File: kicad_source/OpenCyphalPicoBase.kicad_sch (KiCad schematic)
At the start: 48 parts, among them CN1 RASPBERRYPI_PICO, CN11 CONN_02X03, CN12 Conn_01x03, CN2 SM04B-SRSS-TB, CN3 SM04B-SRSS-TB, CN6 691322310002, CN7 CONN_02X03, CN8 Conn_02x08_Odd_Even, SW1 SPST, U3 24LC64

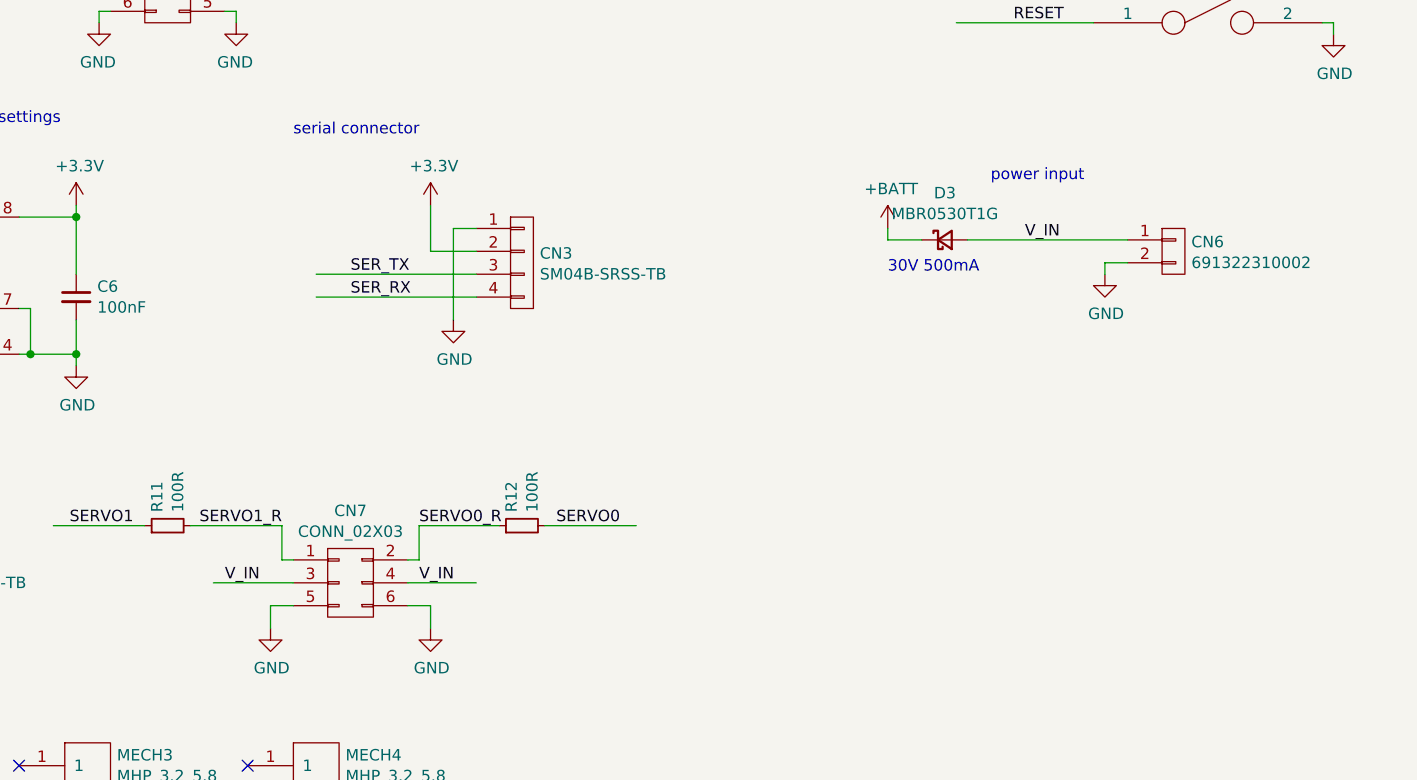
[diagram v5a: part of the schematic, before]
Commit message: switched servos to +BATT to power them from CAN bus
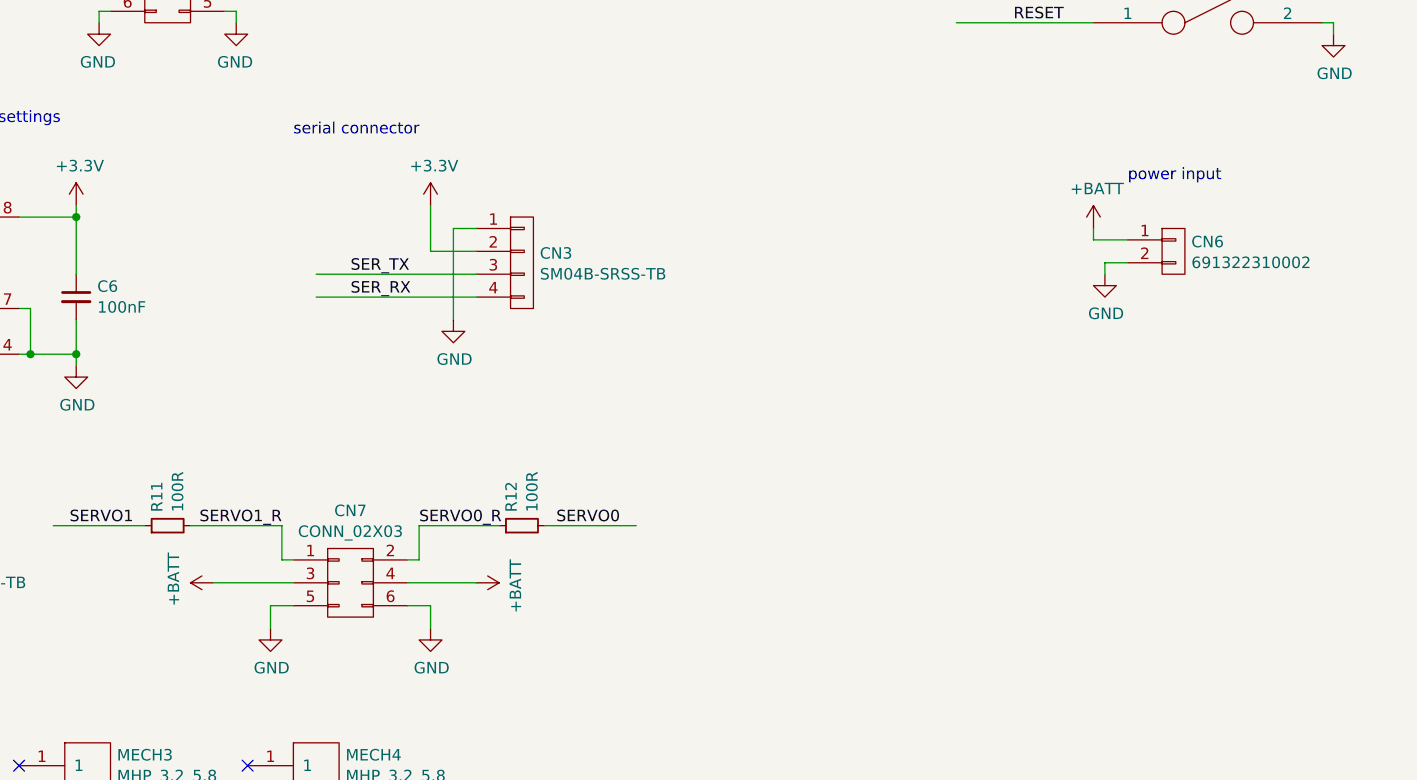
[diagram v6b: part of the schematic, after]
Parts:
- removed D3: MBR0530T1G, Diode_SMD:D_SOD-123, symbol Device:D_Schottky_Small
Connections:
- net V_IN is gone; now on net +BATT: CN6.1 (P1), CN7.3 (P3), CN7.4 (P4)
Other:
- note removed: "30V 500mA"
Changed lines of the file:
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@@
   (title_block
     (title "OpenCyphalPicoBase")
-    (date "2022-10-23")
+    (date "2022-10-24")
     (rev "0.2")
     (company "generationmake")
@@
     (stroke (width 0) (type default) (color 0 0 0 0))
   )
-  (wire (pts (xy 165.1 134.62) (xy 165.1 133.35))
+  (wire (pts (xy 187.96 134.62) (xy 187.96 133.35))
     (stroke (width 0) (type default) (color 0 0 0 0))
   )
@@
     (stroke (width 0) (type default) (color 0 0 0 0))
   )
-  (wire (pts (xy 168.91 134.62) (xy 165.1 134.62))
+  (wire (pts (xy 191.77 134.62) (xy 187.96 134.62))
     (stroke (width 0) (type default) (color 0 0 0 0))
   )
@@
     (stroke (width 0) (type default) (color 0 0 0 0))
   )
-  (wire (pts (xy 191.77 134.62) (xy 173.99 134.62))
-    (stroke (width 0) (type default) (color 0 0 0 0))
-  )
   (wire (pts (xy 116.84 41.91) (xy 116.84 39.37))
     (stroke (width 0) (type default) (color 0 0 0 0))
@@
     (effects (font (size 1.27 1.27)) (justify left bottom))
   )
-  (text "30V 500mA" (at 165.1 138.43 0)
-    (effects (font (size 1.27 1.27)) (justify left bottom))
-  )
   (text "I2C address: 0x50" (at 48.26 124.46 0)
     (effects (font (size 1.27 1.27)) (justify left bottom))
@@
     (effects (font (size 1.27 1.27)) (justify left bottom))
   )
-  (text "power input" (at 176.53 128.27 0)
+  (text "power input" (at 191.77 128.27 0)
     (effects (font (size 1.27 1.27)) (justify left bottom))
   )
@@
     (effects (font (size 1.27 1.27)) (justify left bottom))
   )
-  (label "V_IN" (at 91.44 172.72 0)
-    (effects (font (size 1.27 1.27)) (justify left bottom))
-  )
   (label "RESERVED0" (at 45.72 104.14 180)
     (effects (font (size 1.27 1.27)) (justify right bottom))
@@
     (effects (font (size 1.27 1.27)) (justify left bottom))
   )
-  (label "V_IN" (at 180.34 134.62 0)
-    (effects (font (size 1.27 1.27)) (justify left bottom))
-  )
   (label "SERVO1" (at 81.28 166.37 180)
     (effects (font (size 1.27 1.27)) (justify right bottom))
@@
   (label "OUTPUT1" (at 76.2 66.04 180)
     (effects (font (size 1.27 1.27)) (justify right bottom))
-  )
-  (label "V_IN" (at 113.03 172.72 0)
-    (effects (font (size 1.27 1.27)) (justify left bottom))
   )
   (label "SER_TX" (at 105.41 138.43 0)
@@
     (pin "1")
   )
-  (symbol (lib_id "Device:D_Schottky_Small") (at 171.45 134.62 0) (unit 1)
-    (in_bom yes) (on_board yes)
-    (property "Reference" "D3" (id 0) (at 171.45 129.413 0))
-    (property "Value" "MBR0530T1G" (id 1) (at 171.45 131.7244 0))
-    (property "Footprint" "Diode_SMD:D_SOD-123" (id 2) (at 171.45 134.62 90)
-      (effects (font (size 1.27 1.27)) hide)
-    )
-    (property "Datasheet" "" (id 3) (at 171.45 134.62 90))
-    (pin "1")
-    (pin "2")
-  )
-  (symbol (lib_id "OpenCyphalPicoBase-rescue:+BATT-power-supply") (at 165.1 133.35 0) (unit 1)
-    (in_bom yes) (on_board yes)
-    (property "Reference" "#PWR020" (id 0) (at 165.1 137.16 0)
-      (effects (font (size 1.27 1.27)) hide)
-    )
-    (property "Value" "+BATT" (id 1) (at 165.481 128.9558 0))
-    (property "Footprint" "" (id 2) (at 165.1 133.35 0))
-    (property "Datasheet" "" (id 3) (at 165.1 133.35 0))
+  (symbol (lib_id "OpenCyphalPicoBase-rescue:+BATT-power-supply") (at 187.96 133.35 0) (unit 1)
+    (in_bom yes) (on_board yes)
+    (property "Reference" "#PWR020" (id 0) (at 187.96 137.16 0)
+      (effects (font (size 1.27 1.27)) hide)
+    )
+    (property "Value" "+BATT" (id 1) (at 188.341 128.9558 0))
+    (property "Footprint" "" (id 2) (at 187.96 133.35 0))
+    (property "Datasheet" "" (id 3) (at 187.96 133.35 0))
     (pin "1")
   )
@@
     (pin "3")
   )
+  (symbol (lib_id "OpenCyphalPicoBase-rescue:+BATT-power-supply") (at 119.38 172.72 270) (unit 1)
+    (in_bom yes) (on_board yes)
+    (property "Reference" "#PWR0105" (id 0) (at 115.57 172.72 0)
+      (effects (font (size 1.27 1.27)) hide)
+    )
+    (property "Value" "+BATT" (id 1) (at 123.7742 173.101 0))
+    (property "Footprint" "" (id 2) (at 119.38 172.72 0))
+    (property "Datasheet" "" (id 3) (at 119.38 172.72 0))
+    (pin "1")
+  )
+  (symbol (lib_id "OpenCyphalPicoBase-rescue:+BATT-power-supply") (at 90.17 172.72 90) (unit 1)
+    (in_bom yes) (on_board yes)
+    (property "Reference" "#PWR0104" (id 0) (at 93.98 172.72 0)
+      (effects (font (size 1.27 1.27)) hide)
+    )
+    (property "Value" "+BATT" (id 1) (at 85.7758 172.339 0))
+    (property "Footprint" "" (id 2) (at 90.17 172.72 0))
+    (property "Datasheet" "" (id 3) (at 90.17 172.72 0))
+    (pin "1")
+  )
   (symbol (lib_id "OpenCyphalPicoBase-rescue:+BATT-power-supply") (at 165.1 92.71 0) (unit 1)
     (in_bom yes) (on_board yes)
@@
       (reference "#PWR0103") (unit 1) (value "GND") (footprint "")
     )
+    (path "/7e1637aa-4921-498b-900f-5fdac7ab5374"
+      (reference "#PWR0104") (unit 1) (value "+BATT") (footprint "")
+    )
+    (path "/5573649e-80ef-4e35-960b-dc18f9188f02"
+      (reference "#PWR0105") (unit 1) (value "+BATT") (footprint "")
+    )
     (path "/00000000-0000-0000-0000-000062a11dbe"
       (reference "C1") (unit 1) (value "100nF") (footprint "Capacitor_SMD:C_0603_1608Metric")
@@
       (reference "D2") (unit 1) (value "MBR0530T1G") (footprint "Diode_SMD:D_SOD-123")
     )
-    (path "/00000000-0000-0000-0000-000062533088"
-      (reference "D3") (unit 1) (value "MBR0530T1G") (footprint "Diode_SMD:D_SOD-123")
-    )
     (path "/00000000-0000-0000-0000-000062572e1d"

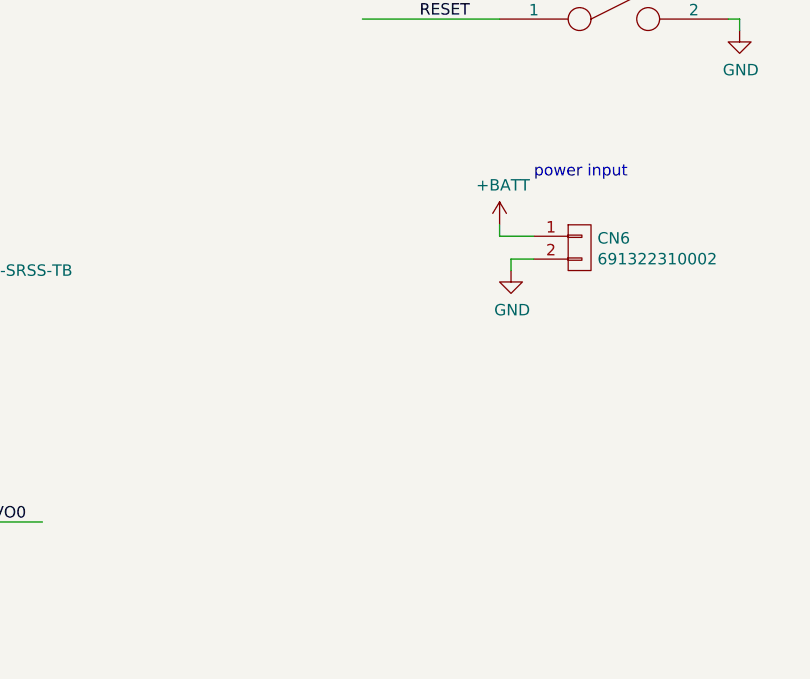
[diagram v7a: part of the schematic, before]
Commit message: added capacitor on +BATT
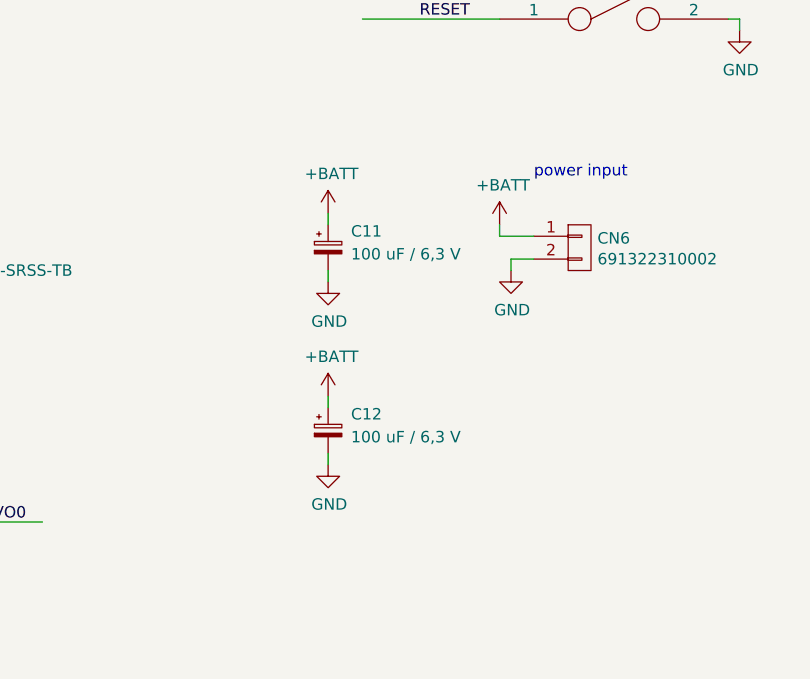
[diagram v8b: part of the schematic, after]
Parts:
- added C11, C12: 100 uF / 6,3 V, Capacitor_SMD:CP_Elec_5x5.3, symbol Device:C_Polarized_Small
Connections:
- net +BATT: now also C11.1, C12.1
- net GND: now also C11.2, C12.2
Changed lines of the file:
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@@
   (title_block
     (title "OpenCyphalPicoBase")
-    (date "2022-10-24")
+    (date "2022-10-26")
     (rev "0.2")
     (company "generationmake")
@@
     (stroke (width 0) (type default) (color 0 0 0 0))
   )
+  (wire (pts (xy 168.91 152.4) (xy 168.91 153.67))
+    (stroke (width 0) (type default) (color 0 0 0 0))
+  )
   (wire (pts (xy 19.05 36.83) (xy 21.59 36.83))
     (stroke (width 0) (type default) (color 0 0 0 0))
@@
     (stroke (width 0) (type default) (color 0 0 0 0))
   )
+  (wire (pts (xy 168.91 138.43) (xy 168.91 139.7))
+    (stroke (width 0) (type default) (color 0 0 0 0))
+  )
   (wire (pts (xy 19.05 41.91) (xy 21.59 41.91))
     (stroke (width 0) (type default) (color 0 0 0 0))
@@
     (stroke (width 0) (type default) (color 0 0 0 0))
   )
+  (wire (pts (xy 168.91 132.08) (xy 168.91 133.35))
+    (stroke (width 0) (type default) (color 0 0 0 0))
+  )
   (wire (pts (xy 256.54 34.29) (xy 265.43 34.29))
     (stroke (width 0) (type default) (color 0 0 0 0))
@@
   )
   (wire (pts (xy 86.36 41.91) (xy 86.36 24.13))
+    (stroke (width 0) (type default) (color 0 0 0 0))
+  )
+  (wire (pts (xy 168.91 158.75) (xy 168.91 160.02))
     (stroke (width 0) (type default) (color 0 0 0 0))
   )
@@
     (pin "1")
   )
+  (symbol (lib_id "Device:C_Polarized_Small") (at 168.91 156.21 0) (unit 1)
+    (in_bom yes) (on_board yes) (fields_autoplaced)
+    (property "Reference" "C12" (id 0) (at 171.45 154.3938 0)
+      (effects (font (size 1.27 1.27)) (justify left))
+    )
+    (property "Value" "100 uF / 6,3 V" (id 1) (at 171.45 156.9338 0)
+      (effects (font (size 1.27 1.27)) (justify left))
+    )
+    (property "Footprint" "Capacitor_SMD:CP_Elec_5x5.3" (id 2) (at 168.91 156.21 0)
+      (effects (font (size 1.27 1.27)) hide)
+    )
+    (property "Datasheet" "~" (id 3) (at 168.91 156.21 0)
+      (effects (font (size 1.27 1.27)) hide)
+    )
+    (pin "1")
+    (pin "2")
+  )
+  (symbol (lib_id "OpenCyphalPicoBase-rescue:GND-power-supply") (at 168.91 139.7 0) (unit 1)
+    (in_bom yes) (on_board yes)
+    (property "Reference" "#PWR014" (id 0) (at 168.91 146.05 0)
+      (effects (font (size 1.27 1.27)) hide)
+    )
+    (property "Value" "GND" (id 1) (at 169.037 144.0942 0))
+    (property "Footprint" "" (id 2) (at 168.91 139.7 0))
+    (property "Datasheet" "" (id 3) (at 168.91 139.7 0))
+    (pin "1")
+  )
+  (symbol (lib_id "OpenCyphalPicoBase-rescue:+BATT-power-supply") (at 168.91 152.4 0) (unit 1)
+    (in_bom yes) (on_board yes)
+    (property "Reference" "#PWR052" (id 0) (at 168.91 156.21 0)
+      (effects (font (size 1.27 1.27)) hide)
+    )
+    (property "Value" "+BATT" (id 1) (at 169.291 148.0058 0))
+    (property "Footprint" "" (id 2) (at 168.91 152.4 0))
+    (property "Datasheet" "" (id 3) (at 168.91 152.4 0))
+    (pin "1")
+  )
   (symbol (lib_id "Connector_Generic:Conn_02x08_Odd_Even") (at 29.21 34.29 0) (mirror y) (unit 1)
     (in_bom yes) (on_board yes) (fields_autoplaced)
@@
     (pin "1")
   )
+  (symbol (lib_id "OpenCyphalPicoBase-rescue:GND-power-supply") (at 168.91 160.02 0) (unit 1)
+    (in_bom yes) (on_board yes)
+    (property "Reference" "#PWR053" (id 0) (at 168.91 166.37 0)
+      (effects (font (size 1.27 1.27)) hide)
+    )
+    (property "Value" "GND" (id 1) (at 169.037 164.4142 0))
+    (property "Footprint" "" (id 2) (at 168.91 160.02 0))
+    (property "Datasheet" "" (id 3) (at 168.91 160.02 0))
+    (pin "1")
+  )
+  (symbol (lib_id "OpenCyphalPicoBase-rescue:+BATT-power-supply") (at 168.91 132.08 0) (unit 1)
+    (in_bom yes) (on_board yes)
+    (property "Reference" "#PWR08" (id 0) (at 168.91 135.89 0)
+      (effects (font (size 1.27 1.27)) hide)
+    )
+    (property "Value" "+BATT" (id 1) (at 169.291 127.6858 0))
+    (property "Footprint" "" (id 2) (at 168.91 132.08 0))
+    (property "Datasheet" "" (id 3) (at 168.91 132.08 0))
+    (pin "1")
+  )
   (symbol (lib_id "OpenCyphalPicoBase-rescue:+BATT-power-supply") (at 165.1 92.71 0) (unit 1)
     (in_bom yes) (on_board yes)
@@
     (property "Datasheet" "" (id 3) (at 165.1 92.71 0))
     (pin "1")
+  )
+  (symbol (lib_id "Device:C_Polarized_Small") (at 168.91 135.89 0) (unit 1)
+    (in_bom yes) (on_board yes) (fields_autoplaced)
+    (property "Reference" "C11" (id 0) (at 171.45 134.0738 0)
+      (effects (font (size 1.27 1.27)) (justify left))
+    )
+    (property "Value" "100 uF / 6,3 V" (id 1) (at 171.45 136.6138 0)
+      (effects (font (size 1.27 1.27)) (justify left))
+    )
+    (property "Footprint" "Capacitor_SMD:CP_Elec_5x5.3" (id 2) (at 168.91 135.89 0)
+      (effects (font (size 1.27 1.27)) hide)
+    )
+    (property "Datasheet" "~" (id 3) (at 168.91 135.89 0)
+      (effects (font (size 1.27 1.27)) hide)
+    )
+    (pin "1")
+    (pin "2")
   )
   (symbol (lib_id "OpenCyphalPicoBase-rescue:CONN_02X03-mechanical-connectors") (at 85.09 106.68 0) (mirror y) (unit 1)
@@
       (reference "#PWR07") (unit 1) (value "+3.3V") (footprint "")
     )
+    (path "/d243c880-d322-4872-ae06-62caa86c5823"
+      (reference "#PWR08") (unit 1) (value "+BATT") (footprint "")
+    )
     (path "/00000000-0000-0000-0000-000062a14cc6"
       (reference "#PWR09") (unit 1) (value "GND") (footprint "")
@@
       (reference "#PWR013") (unit 1) (value "GND") (footprint "")
     )
+    (path "/19a7c858-5698-4445-8d4f-5fce6b87fd79"
+      (reference "#PWR014") (unit 1) (value "GND") (footprint "")
+    )
     (path "/00000000-0000-0000-0000-00006254a49e"
       (reference "#PWR015") (unit 1) (value "+BATT") (footprint "")
@@
       (reference "#PWR051") (unit 1) (value "GND") (footprint "")
     )
+    (path "/1b9ed98e-9794-43b6-9513-6b70efa279c6"
+      (reference "#PWR052") (unit 1) (value "+BATT") (footprint "")
+    )
+    (path "/c3979e04-2e0c-4de7-a444-c8166b6cadd1"
+      (reference "#PWR053") (unit 1) (value "GND") (footprint "")
+    )
     (path "/00000000-0000-0000-0000-000062c052ff"
       (reference "#PWR054") (unit 1) (value "GND") (footprint "")
@@
       (reference "C10") (unit 1) (value "100nF") (footprint "Capacitor_SMD:C_0603_1608Metric")
     )
+    (path "/d51d71ed-f6c3-4dba-8462-257557601dd4"
+      (reference "C11") (unit 1) (value "100 uF / 6,3 V") (footprint "Capacitor_SMD:CP_Elec_5x5.3")
+    )
+    (path "/0c3f626b-e5ab-4546-95f5-05afc50b086b"
+      (reference "C12") (unit 1) (value "100 uF / 6,3 V") (footprint "Capacitor_SMD:CP_Elec_5x5.3")
+    )
     (path "/00000000-0000-0000-0000-0000629e332f"
